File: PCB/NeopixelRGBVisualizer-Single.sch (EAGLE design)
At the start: 23 parts, among them CN2 5-12VDC, IC1 MSGEQ7, IC2 78L05ACZ-AP, Q1 16MHz, X1 STEREOJACK

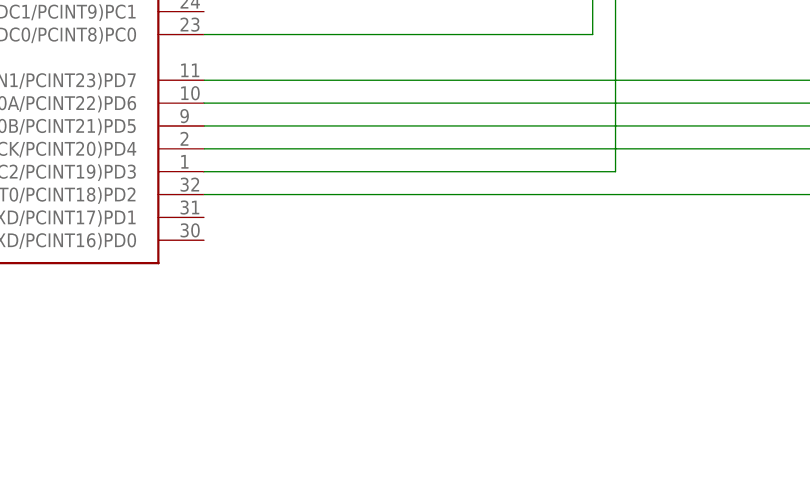
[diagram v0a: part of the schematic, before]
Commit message: Added headers to access serial TX/RX pins, power, and GND.  Requried 2 more vias.
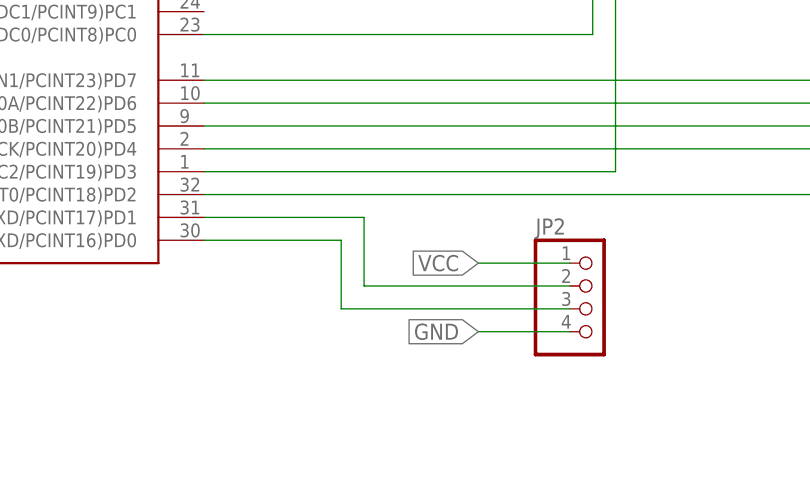
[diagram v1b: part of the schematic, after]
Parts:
- added JP2: (no value), mypinhead:PINHD-1X4/OCT
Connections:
- new net RX: JP2.3, U$1.(RXD/PCINT16)PD0
- new net TX: JP2.2, U$1.(TXD/PCINT17)PD1
- net GND: now also JP2.4
- net VCC: now also JP2.1
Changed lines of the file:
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@@
 <part name="U$3" library="MinifitJR" deviceset="0039303035" device=""/>
 <part name="JP1" library="mypinhead" deviceset="PINHD-1X2" device="/ROUND" value="1/0"/>
+<part name="JP2" library="mypinhead" deviceset="PINHD-1X4" device="/OCT"/>
 </parts>
 <sheets>
@@
 <attribute name="NAME" x="176.53" y="36.195" size="1.778" layer="95"/>
 <attribute name="VALUE" x="176.53" y="25.4" size="1.778" layer="96"/>
+</instance>
+<instance part="JP2" gate="A" x="116.84" y="0">
+<attribute name="NAME" x="110.49" y="8.255" size="1.778" layer="95"/>
+<attribute name="VALUE" x="110.49" y="-7.62" size="1.778" layer="96"/>
 </instance>
 </instances>
@@
 <junction x="193.04" y="20.32"/>
 </segment>
+<segment>
+<pinref part="JP2" gate="A" pin="4"/>
+<wire x1="114.3" y1="-2.54" x2="104.14" y2="-2.54" width="0.1524" layer="91"/>
+<label x="104.14" y="-2.54" size="1.778" layer="95" rot="R180" xref="yes"/>
+</segment>
 </net>
 <net name="N$10" class="0">
@@
 <pinref part="IC2" gate="1" pin="OUT"/>
 </segment>
+<segment>
+<pinref part="JP2" gate="A" pin="1"/>
+<wire x1="114.3" y1="5.08" x2="104.14" y2="5.08" width="0.1524" layer="91"/>
+<label x="104.14" y="5.08" size="1.778" layer="95" rot="R180" xref="yes"/>
+</segment>
 </net>
 <net name="N$16" class="0">
@@
 </segment>
 </net>
+<net name="TX" class="0">
+<segment>
+<pinref part="U$1" gate="G$1" pin="(TXD/PCINT17)PD1"/>
+<wire x1="73.66" y1="10.16" x2="91.44" y2="10.16" width="0.1524" layer="91"/>
+<wire x1="91.44" y1="10.16" x2="91.44" y2="2.54" width="0.1524" layer="91"/>
+<pinref part="JP2" gate="A" pin="2"/>
+<wire x1="91.44" y1="2.54" x2="114.3" y2="2.54" width="0.1524" layer="91"/>
+</segment>
+</net>
+<net name="RX" class="0">
+<segment>
+<pinref part="U$1" gate="G$1" pin="(RXD/PCINT16)PD0"/>
+<wire x1="73.66" y1="7.62" x2="88.9" y2="7.62" width="0.1524" layer="91"/>
+<wire x1="88.9" y1="7.62" x2="88.9" y2="0" width="0.1524" layer="91"/>
+<pinref part="JP2" gate="A" pin="3"/>
+<wire x1="88.9" y1="0" x2="114.3" y2="0" width="0.1524" layer="91"/>
+</segment>
+</net>
